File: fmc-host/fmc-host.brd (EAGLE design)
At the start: 76.5 x 69 mm, 307 parts, among them J1 SMA002, J2 SMA002, J3 SMA002, J4 SMA002, J5 SMA002, J6 ESHF-105-01-L-D-SM-K-TR, J7 12226-8250-00FR, J8 FMC_SINGLE_WIDTH_MODULE, J9 ASP-134488-01, Q1 SI1012R, Q2 SI1012R, U1 SN74LVC2G34DCKR, U10 DS90UB934-Q1, U11 DS91M040, U12 AD5766BCPZ-RL7, U13 MCP47FEB02A0-E/ST, U14 LM4132AMF-2.5/NOPBCT-ND, U15 AD7617BSTZ, U16 AD5142BCPZ10, U17 LTM4622A, U19 TPS7A49, U2 SN65LVDS9638DGN, U20 TPS7A49, U21 TPS7A30, U22 24AA64ST, U23 LTM8049_BGA, U24 TPS62061DSGT, U3 FIN1032MTCX, U4 ADCMP600, U5 ADCMP600, U6 DG1412E, U7 DG1412E, U8 DG1412E, U9 DS90UB934-Q1, X2 OE-LOGO_7X5

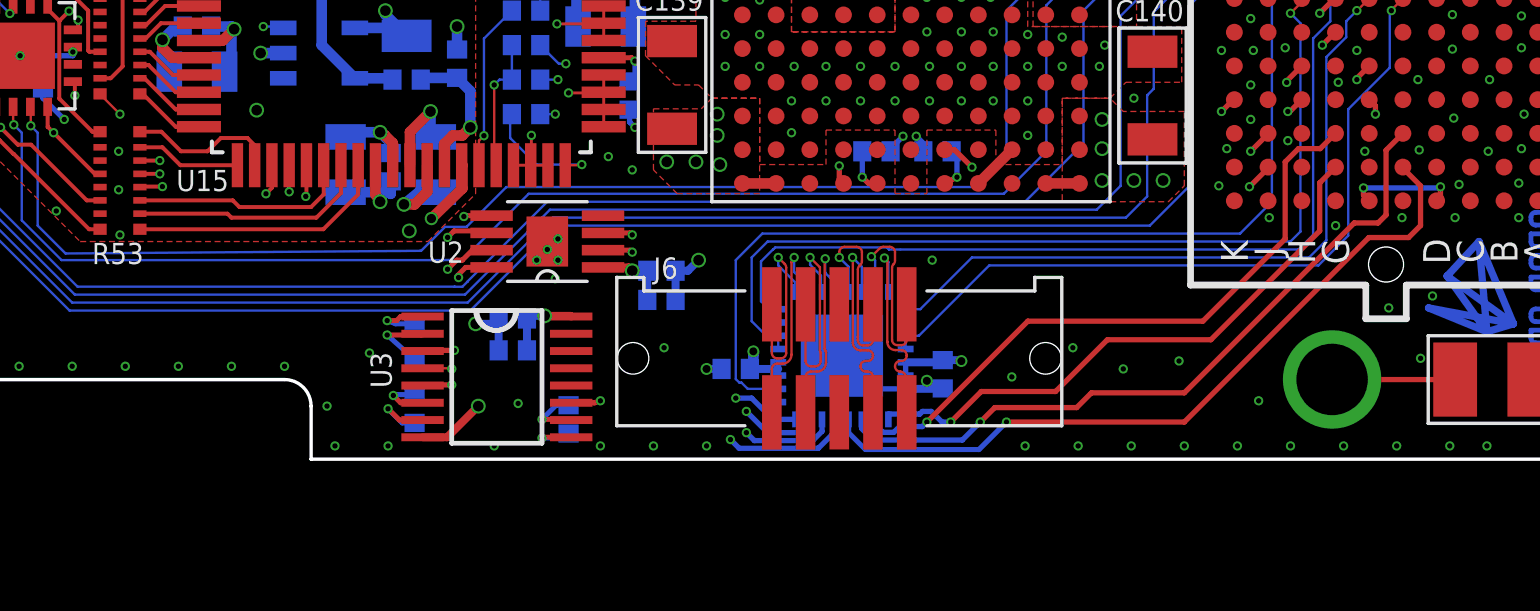
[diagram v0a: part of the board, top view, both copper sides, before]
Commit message: Revision 1.6
- The major change here is that I've swapped the vertical MVLVDS sync
header for a through-hole right-angle version that is much more
amenable to daisy chain connections when the card is in a PCIe slot.
- Deleted some obsolete, hard to maintain files
- Deleted some obsolete datasheets
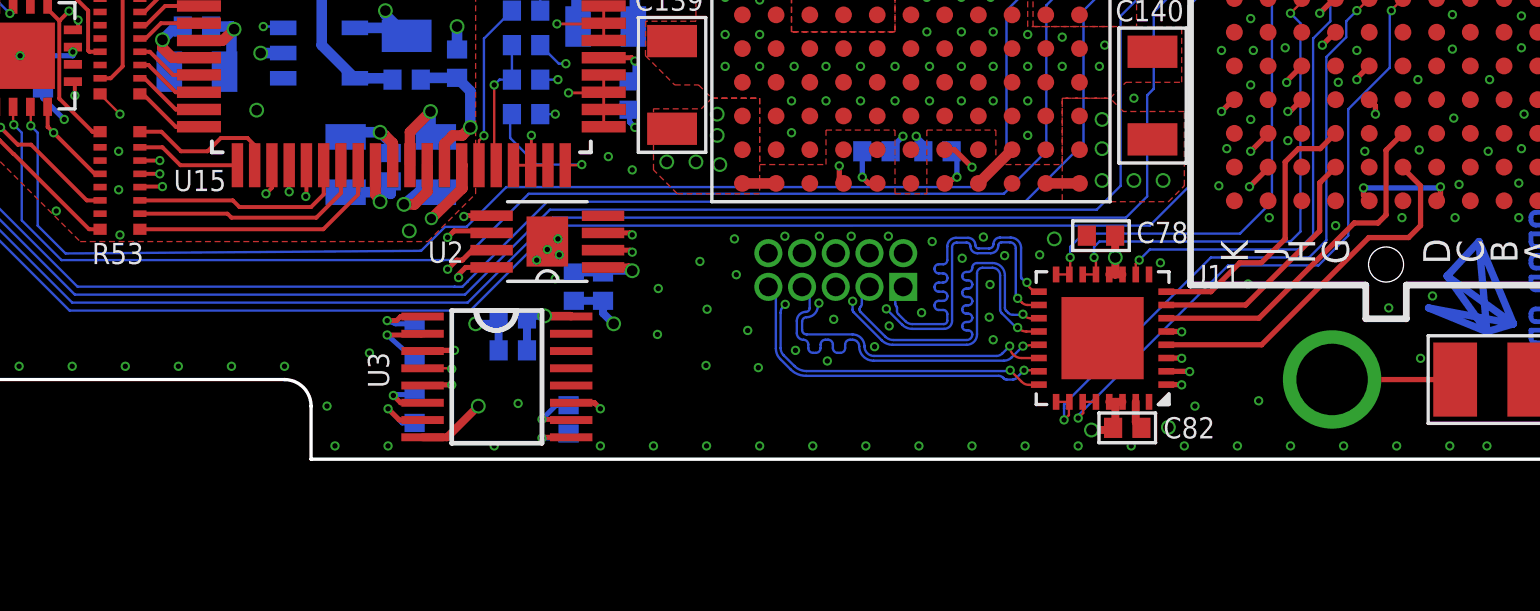
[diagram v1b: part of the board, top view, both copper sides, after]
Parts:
- J6: value ESHF-105-01-L-D-SM-K-TR -> FTSH-105-01-F-D-RA-K; device jonnew:ESHF-105-01-L-D-SM-K-TR -> jonnew:FTSH-105-01-F-D-RA-K
- moved C78 14.6 mm to (-8.74, 5.42), flipped to the top, turned to 0 degrees
- moved U11 9.84 mm to (-8.68, 1.56), flipped to the top, turned to 270 degrees
- moved C82 7.24 mm to (-7.75, -1.82), flipped to the top, turned to 180 degrees
- moved C32 3.34 mm to (-28.6, 3.50), turned to 270 degrees
- moved J6 3.33 mm to (-18.7, 4.13), flipped to the bottom, turned to 180 degrees
- moved C28 2.28 mm to (-27.5, 3.50), turned to 270 degrees
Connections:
- net MLDVS_RO2 renamed MLVDS_RO2
- removed net MLDVS_EN: J9.H8, U11.10
- removed net MLDVS_RO0: J9.G2, U11.1
- removed net MLDVS_RO1: J9.E3, U11.3
- removed net MLDVS_RO3: J9.F4, U11.7
- new net MLVDS_EN: J9.F8, U11.10
- new net MLVDS_RO0: J9.F4, U11.1
- new net MLVDS_RO1: J9.G6, U11.3
- new net MLVDS_RO3: J9.G2, U11.7
- net MLVDS_CLK_0_N: now also J6.10; no longer J6.9
- net MLVDS_CLK_0_P: now also J6.09; no longer J6.10
- net MLVDS_CLK_1_N: now also J6.08; no longer J6.7
- net MLVDS_CLK_1_P: now also J6.07; no longer J6.8
- net MLVDS_CLK_2_N: now also J6.04; no longer J6.3
- net MLVDS_CLK_2_P: now also J6.03; no longer J6.4
- net MLVDS_CLK_3_N: now also J6.02; no longer J6.1
- net MLVDS_CLK_3_P: now also J6.01; no longer J6.2
- net MLVDS_DE_!RE3: now also J9.H8; no longer J9.F8
- net MLVDS_DI0: now also J9.F5; no longer J9.G3
- net MLVDS_DI2: now also J9.E3; no longer J9.G6
- net MLVDS_DI3: now also J9.G3; no longer J9.F5
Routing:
- net MLDVS_EN: track 36.7 -> 0.00 mm, vias 1 -> 0
- net MLDVS_RO3: track 34.7 -> 0.00 mm, vias 2 -> 0
- net MLDVS_RO1: track 27.1 -> 0.00 mm, vias 1 -> 0
- net MLVDS_RO2: track 42.8 -> 15.8 mm
- net MLVDS_DI2: track 38.7 -> 13.2 mm, vias 2 -> 0
- net MLVDS_DI3: track 34.8 -> 10.5 mm, vias 2 -> 0
- net MLDVS_RO0: track 22.3 -> 0.00 mm, vias 1 -> 0
- net MLVDS_EN: track 0.00 -> 18.6 mm, vias 0 -> 2
- net MLVDS_DE_!RE3: track 35.1 -> 19.2 mm, vias 1 -> 2
- net MLVDS_DE_!RE2: track 34.3 -> 18.7 mm, vias 1 -> 2
- net MLVDS_RO1: track 0.00 -> 15.5 mm, vias 0 -> 2
- net MLVDS_RO0: track 0.00 -> 15.3 mm, vias 0 -> 2
- net MLVDS_DI1: track 28.3 -> 13.9 mm, vias 1 -> 0
- net MLVDS_RO3: track 0.00 -> 9.59 mm
- net MLVDS_DI0: track 24.0 -> 15.6 mm, vias 1 -> 2
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- added copper zone on layer 5, net GND
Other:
- board text added: "Rev. 1.6 JPN 2021"
- board text added: "SYNC"
- board text removed: "Rev. 1.5 JPN 2020"

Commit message: Revision F ready for fabrication feedback
- Replaced QFN AD5142 with TSSOP package, which is available
- Added ground pours to all layers
- Used thermals on top and bottom to improve solderability
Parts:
- removed D7, D8: APFA3011-AK13/F, jonnew:RGB_LED_SMD-6
- added J10: BM08B-SURS-TF, jonnew:BM08B-SURS-TF
- C133, C136: value 47uF -> 33uF; device jonnew:1210 -> jonnew:1411-VISHAY-B
- U16: device jonnew:CP_16_27-L -> jonnew:TSSOP-16_4.4X5.0
- moved R45 57.7 mm to (-7.40, 26.7)
- moved R47 57.3 mm to (-7.40, 28.9)
- moved R42 56.6 mm to (-7.40, 27.8), turned to 0 degrees
- moved R46 56.5 mm to (-7.40, 25.6)
- moved R44 56.4 mm to (-7.40, 24.5)
- moved R41 53.9 mm to (-7.40, 30.0)
- moved R49 37.8 mm to (-19.7, 36.9), flipped to the top
- moved R51 37.7 mm to (-19.7, 38.3), flipped to the top
- moved R52 31.5 mm to (-25.4, 46.4), flipped to the top
- moved R50 30.8 mm to (-25.4, 47.7), flipped to the top
- moved C126 2.30 mm to (-18.1, 23.4), turned to 0 degrees
- moved C125 2.30 mm to (-12.6, 23.1), turned to 0 degrees
- moved C120 1.90 mm to (-17.6, 32.6)
- moved C124 1.90 mm to (-25.1, 25.2)
- moved R75 1.90 mm to (-24.8, 30.8)
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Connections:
- removed net DES_A_LEDG: J9.F28, R47.2
- removed net DES_B_LEDG: J9.G21, R46.2
- removed net N$118: D7.1, R41.1
- removed net N$119: D7.2, R44.1
- removed net N$16: D8.4, R47.1
- removed net N$26: D7.4, R46.1
- removed net N$53: D8.1, R42.1
- new net N$101: J10.4, R45.1
- new net N$102: J10.3, R46.1
- new net N$103: J10.1, R44.1
- new net N$57: J10.7, R47.1
- new net N$66: J10.8, R41.1
- new net PORT_A_BLUE: J9.G18, R41.2
- new net PORT_A_GREEN: J9.J18, R47.2
- new net PORT_A_RED: J9.H17, R42.1
- new net PORT_B_BLUE: J9.H16, R45.2
- new net PORT_B_GREEN: J9.G15, R46.2
- new net PORT_B_RED: J9.G13, R44.2
- net !LINK_PWR_ADJ_CS: now also U16.16; no longer U16.14
- net !LINK_PWR_ADJ_RESET: now also U16.2; no longer U16.16
- net +12V: now also C133.A; no longer C133.2
- net +3V3: now also C136.A, U16.1, U16.11, U16.12; no longer C136.2, U16.10, U16.15, U16.9
- net AIN_AOUT9: now also J9.J19; no longer J9.J18
- net DES_A_LOCK: no longer R42.2
- net DES_A_PASS: no longer R45.2
- net DES_B_LOCK: no longer R41.2
- net DES_B_PASS: no longer R44.2
- net GND: now also C133.C, C136.C, J10.2, J10.6, U16.9; no longer C133.1, C136.1, D7.3, D7.5, D7.6, D8.3, D8.5, D8.6, U16.1, U16.PAD
- net LINK_PWR_ADJ_MISO: now also U16.15; no longer U16.13
- net LINK_PWR_ADJ_MOSI: now also U16.14; no longer U16.12
- net LINK_PWR_ADJ_SCLK: now also U16.13; no longer U16.11
- net N$122: now also U16.4; no longer U16.2
- net N$123: now also U16.8; no longer U16.6
- net N$54: now also J10.5, R42.2; no longer D8.2, R45.1
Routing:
- net GND: track 130.0 -> 25.1 mm, vias 730 -> 728
- net DES_B_LEDG: track 70.0 -> 0.00 mm, vias 2 -> 0
- net DES_A_LEDG: track 66.4 -> 0.00 mm, vias 2 -> 0
- net DES_B_PASS: track 68.5 -> 21.5 mm
- net DES_B_LOCK: track 68.2 -> 21.6 mm
- net DES_A_LOCK: track 74.9 -> 49.7 mm
- net DES_A_PASS: track 68.7 -> 46.3 mm
- net PORT_A_BLUE: track 0.00 -> 8.83 mm, vias 0 -> 1
- net PORT_B_RED: track 0.00 -> 8.01 mm, vias 0 -> 1
- net PORT_B_GREEN: track 0.00 -> 7.46 mm, vias 0 -> 1
- net PORT_A_RED: track 0.00 -> 6.92 mm, vias 0 -> 1
- net PORT_B_BLUE: track 0.00 -> 6.36 mm, vias 0 -> 1
- net !LINK_PWR_ADJ_RESET: track 15.1 -> 21.0 mm
- net LINK_PWR_ADJ_MISO: track 12.5 -> 17.6 mm, vias 2 -> 3
- net N$103: track 0.00 -> 5.14 mm, vias 0 -> 1
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- added copper zone on layer 3, net GND
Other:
- board size 76.5 x 69 mm -> 76.5 x 339.8 mm
- board text added: "Mill out"
- board text added: "Panel by fab."
- board text added: "Rev. F JPN 2021"
- board text added: "V-CUT"
- board text removed: "Rev. 1.6 JPN 2021"
